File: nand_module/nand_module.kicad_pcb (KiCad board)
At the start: 2 copper layers, 47.1 x 30.9 mm, 19 parts, among them J1 BUS_A, J2 BUS_B

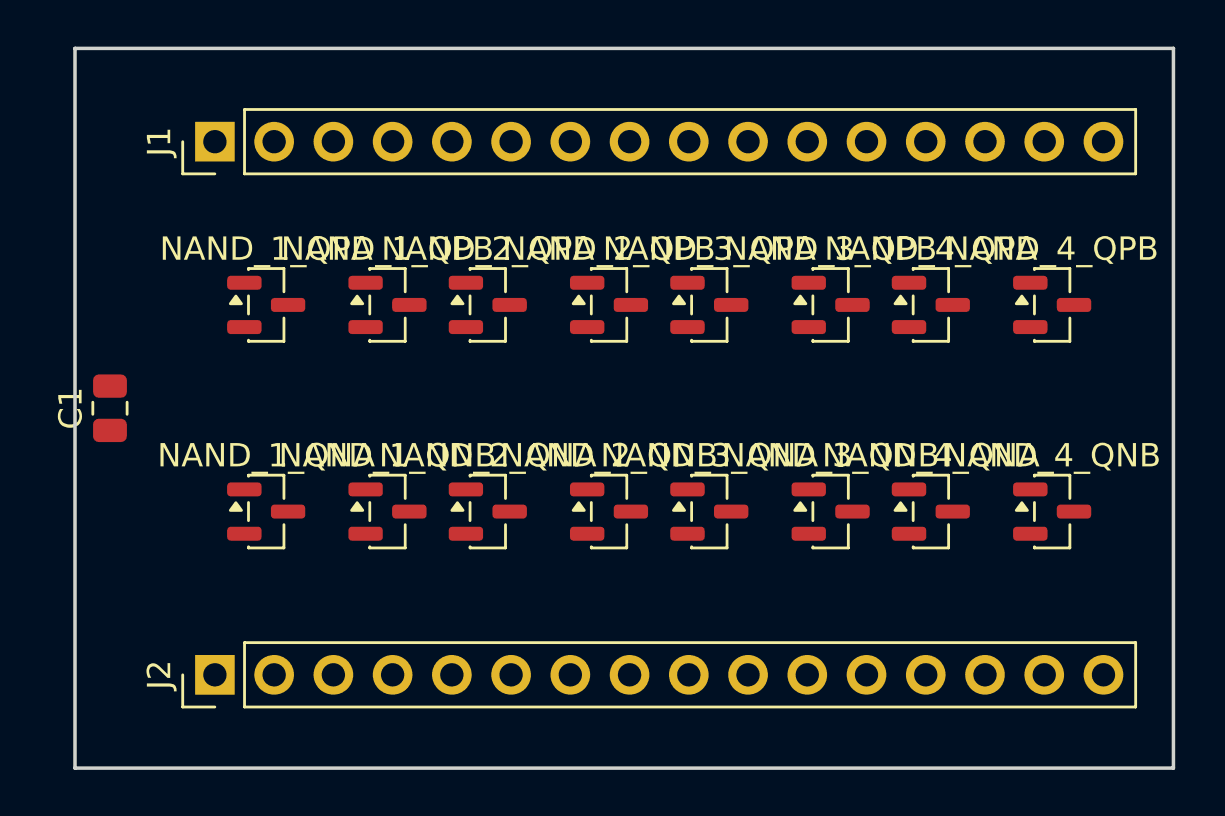
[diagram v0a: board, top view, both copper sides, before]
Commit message: Route NAND module (2-layer, top)
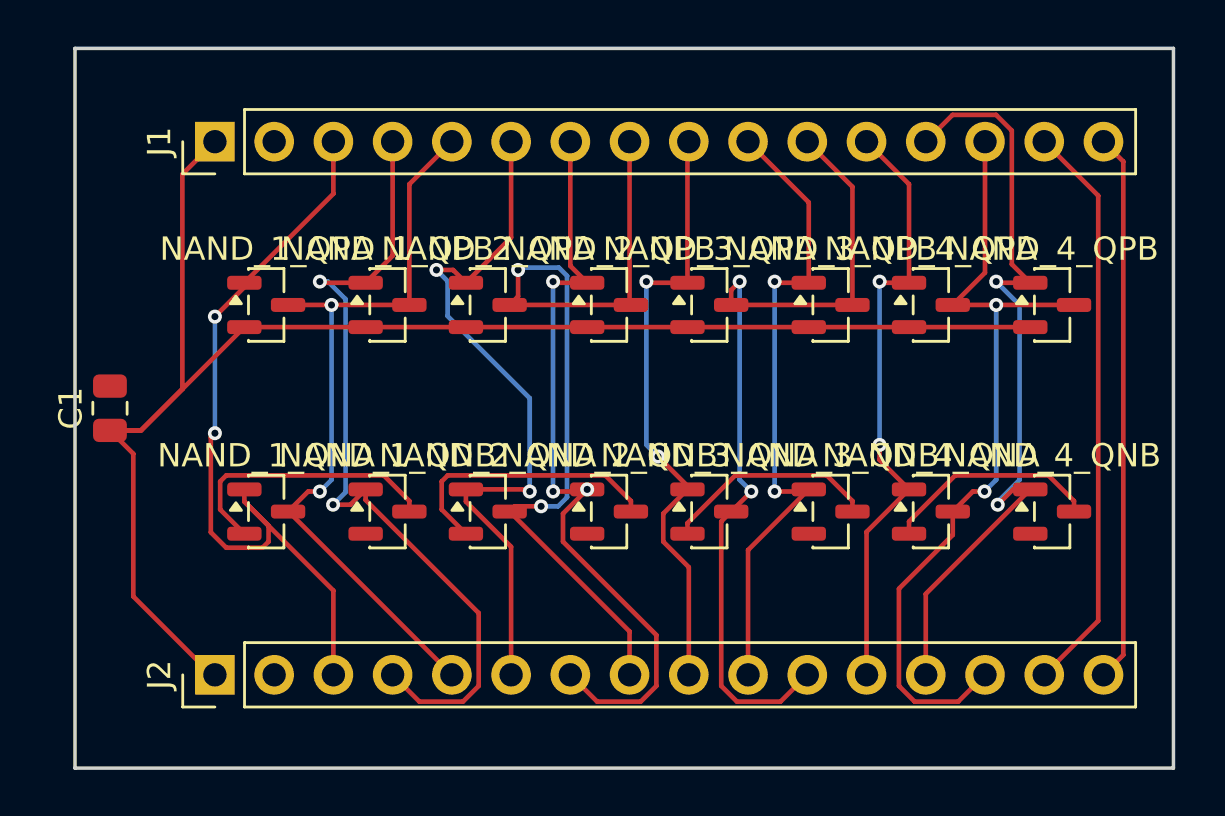
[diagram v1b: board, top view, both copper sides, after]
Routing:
- net VDD: track 0.00 -> 68.7 mm
- net NAND_2_Y: track 0.00 -> 37.5 mm, vias 0 -> 2
- net NAND_3_Y: track 0.00 -> 36.7 mm, vias 0 -> 2
- net NAND_4_Y: track 0.00 -> 35.6 mm, vias 0 -> 2
- net NAND_1_B: track 0.00 -> 35.5 mm, vias 0 -> 2
- net NAND_4_B: track 0.00 -> 34.7 mm, vias 0 -> 2
- net NAND_1_A: track 0.00 -> 33.5 mm, vias 0 -> 2
- net NAND_2_B: track 0.00 -> 33.3 mm, vias 0 -> 3
- net NAND_1_Y: track 0.00 -> 32.8 mm, vias 0 -> 2
- net NAND_2_A: track 0.00 -> 31.0 mm, vias 0 -> 2
- net NAND_3_B: track 0.00 -> 28.1 mm, vias 0 -> 2
- net NAND_3_A: track 0.00 -> 26.3 mm, vias 0 -> 2
- net NAND_4_A: track 0.00 -> 26.2 mm, vias 0 -> 2
- net BUS_X: track 0.00 -> 24.8 mm
- net BUS_Y: track 0.00 -> 23.6 mm
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
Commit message: Rename NAND board refs to short scheme; drop rename_refs.py
Ran rename_refs.py (kept in history at fabc05a) over the routed board:
NAND_<n>_QP*/QN* -> QP*_<n>/QN*_<n>. 240 track objects and all net
names verified unchanged. Also captures routing progress (211 segments).
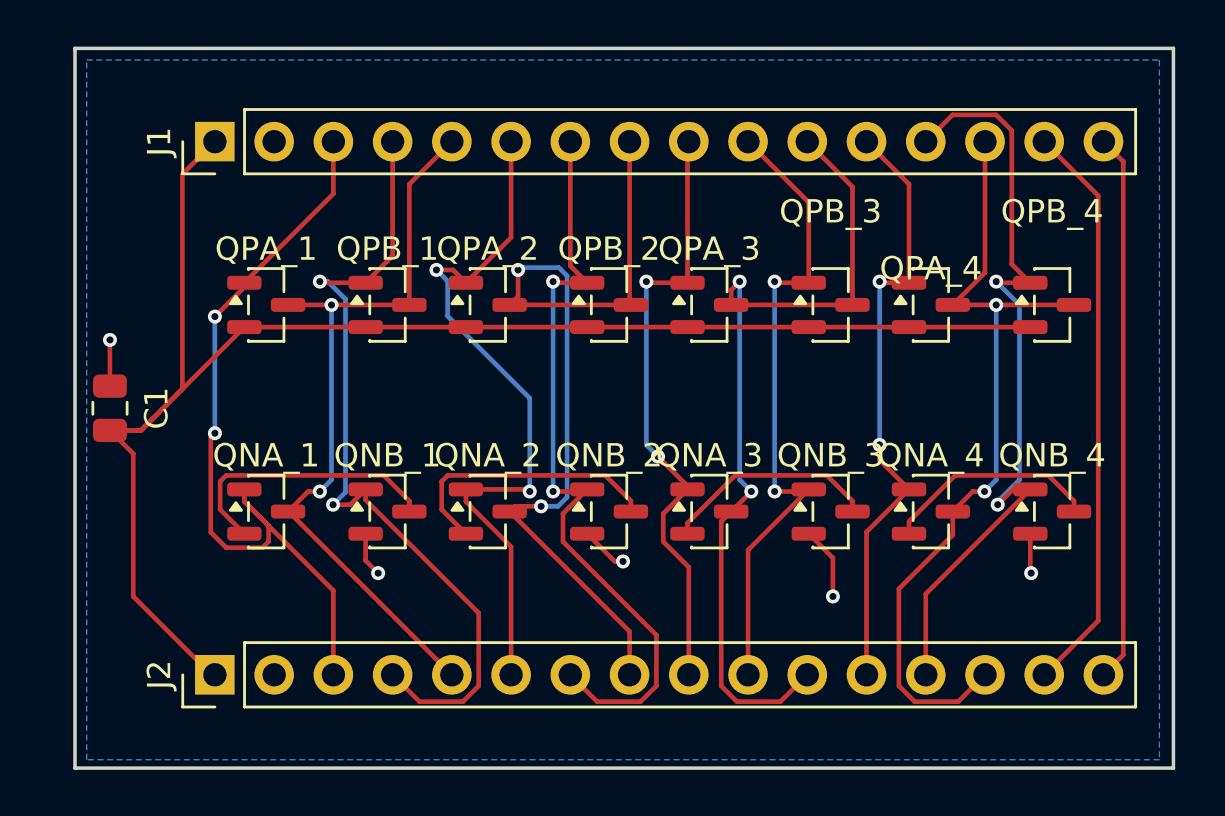
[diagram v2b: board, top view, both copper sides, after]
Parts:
- renumbered NAND_1_QNA to QNA_1, NAND_2_QNA to QNA_2, NAND_3_QNA to QNA_3, NAND_4_QNA to QNA_4, NAND_1_QNB to QNB_1, NAND_2_QNB to QNB_2, NAND_3_QNB to QNB_3, NAND_4_QNB to QNB_4, NAND_1_QPA to QPA_1, NAND_2_QPA to QPA_2, NAND_3_QPA to QPA_3, NAND_4_QPA to QPA_4, NAND_1_QPB to QPB_1, NAND_2_QPB to QPB_2, NAND_3_QPB to QPB_3, NAND_4_QPB to QPB_4
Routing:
- net GND: track 0.00 -> 10.7 mm, vias 0 -> 5
- net NAND_2_B: vias 3 -> 2
- added copper zone on B.Cu, net GND
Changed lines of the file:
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@@
 		(descr "SOT, 3 Pin (JEDEC TO-236 Var AB https://www.jedec.org/document_search?search_api_views_fulltext=TO-236)")
 		(tags "SOT TO_SOT_SMD")
-		(property "Reference" "NAND_2_QPA"
+		(property "Reference" "QPA_2"
 			(at 0 -2.4 0)
 			(layer "F.SilkS")
@@
 		(descr "SOT, 3 Pin (JEDEC TO-236 Var AB https://www.jedec.org/document_search?search_api_views_fulltext=TO-236)")
 		(tags "SOT TO_SOT_SMD")
-		(property "Reference" "NAND_4_QNA"
+		(property "Reference" "QNA_4"
 			(at 0 -2.4 0)
 			(layer "F.SilkS")
@@
 		(descr "SOT, 3 Pin (JEDEC TO-236 Var AB https://www.jedec.org/document_search?search_api_views_fulltext=TO-236)")
 		(tags "SOT TO_SOT_SMD")
-		(property "Reference" "NAND_3_QNB"
+		(property "Reference" "QNB_3"
 			(at 0 -2.4 0)
 			(layer "F.SilkS")
@@
 		(descr "SOT, 3 Pin (JEDEC TO-236 Var AB https://www.jedec.org/document_search?search_api_views_fulltext=TO-236)")
 		(tags "SOT TO_SOT_SMD")
-		(property "Reference" "NAND_2_QNB"
+		(property "Reference" "QNB_2"
 			(at 0 -2.4 0)
 			(layer "F.SilkS")
@@
 		(descr "SOT, 3 Pin (JEDEC TO-236 Var AB https://www.jedec.org/document_search?search_api_views_fulltext=TO-236)")
 		(tags "SOT TO_SOT_SMD")
-		(property "Reference" "NAND_3_QPB"
-			(at 0 -2.4 0)
+		(property "Reference" "QPB_3"
+			(at 0 -4 0)
 			(layer "F.SilkS")
 			(effects
@@
 		(descr "SOT, 3 Pin (JEDEC TO-236 Var AB https://www.jedec.org/document_search?search_api_views_fulltext=TO-236)")
 		(tags "SOT TO_SOT_SMD")
-		(property "Reference" "NAND_1_QNB"
+		(property "Reference" "QNB_1"
 			(at 0 -2.4 0)
 			(layer "F.SilkS")
@@
 		(descr "SOT, 3 Pin (JEDEC TO-236 Var AB https://www.jedec.org/document_search?search_api_views_fulltext=TO-236)")
 		(tags "SOT TO_SOT_SMD")
-		(property "Reference" "NAND_1_QNA"
+		(property "Reference" "QNA_1"
 			(at 0 -2.4 0)
 			(layer "F.SilkS")
@@
 		(descr "SOT, 3 Pin (JEDEC TO-236 Var AB https://www.jedec.org/document_search?search_api_views_fulltext=TO-236)")
 		(tags "SOT TO_SOT_SMD")
-		(property "Reference" "NAND_3_QNA"
+		(property "Reference" "QNA_3"
 			(at 0 -2.4 0)
 			(layer "F.SilkS")
@@
 		(descr "SOT, 3 Pin (JEDEC TO-236 Var AB https://www.jedec.org/document_search?search_api_views_fulltext=TO-236)")
 		(tags "SOT TO_SOT_SMD")
-		(property "Reference" "NAND_1_QPA"
+		(property "Reference" "QPA_1"
 			(at 0 -2.4 0)
 			(layer "F.SilkS")
@@
 		(descr "SOT, 3 Pin (JEDEC TO-236 Var AB https://www.jedec.org/document_search?search_api_views_fulltext=TO-236)")
 		(tags "SOT TO_SOT_SMD")
-		(property "Reference" "NAND_2_QNA"
+		(property "Reference" "QNA_2"
 			(at 0 -2.4 0)
 			(layer "F.SilkS")
@@
 		(descr "SOT, 3 Pin (JEDEC TO-236 Var AB https://www.jedec.org/document_search?search_api_views_fulltext=TO-236)")
 		(tags "SOT TO_SOT_SMD")
-		(property "Reference" "NAND_3_QPA"
+		(property "Reference" "QPA_3"
 			(at 0 -2.4 0)
 			(layer "F.SilkS")
@@
 		(descr "SOT, 3 Pin (JEDEC TO-236 Var AB https://www.jedec.org/document_search?search_api_views_fulltext=TO-236)")
 		(tags "SOT TO_SOT_SMD")
-		(property "Reference" "NAND_4_QNB"
+		(property "Reference" "QNB_4"
 			(at 0 -2.4 0)
 			(layer "F.SilkS")
@@
 		(tags "capacitor")
 		(property "Reference" "C1"
-			(at 0 -1.68 90)
+			(at 0 2 90)
 			(layer "F.SilkS")
 			(effects
@@
 		(descr "SOT, 3 Pin (JEDEC TO-236 Var AB https://www.jedec.org/document_search?search_api_views_fulltext=TO-236)")
 		(tags "SOT TO_SOT_SMD")
-		(property "Reference" "NAND_4_QPA"
-			(at 0 -2.4 0)
+		(property "Reference" "QPA_4"
+			(at 0 -1.56 0)
 			(layer "F.SilkS")
 			(effects
@@
 		(descr "SOT, 3 Pin (JEDEC TO-236 Var AB https://www.jedec.org/document_search?search_api_views_fulltext=TO-236)")
 		(tags "SOT TO_SOT_SMD")
-		(property "Reference" "NAND_1_QPB"
+		(property "Reference" "QPB_1"
 			(at 0 -2.4 0)
 			(layer "F.SilkS")
@@
 		(descr "SOT, 3 Pin (JEDEC TO-236 Var AB https://www.jedec.org/document_search?search_api_views_fulltext=TO-236)")
 		(tags "SOT TO_SOT_SMD")
-		(property "Reference" "NAND_4_QPB"
-			(at 0 -2.4 0)
+		(property "Reference" "QPB_4"
+			(at 0 -4 0)
 			(layer "F.SilkS")
 			(effects
@@
 		(descr "SOT, 3 Pin (JEDEC TO-236 Var AB https://www.jedec.org/document_search?search_api_views_fulltext=TO-236)")
 		(tags "SOT TO_SOT_SMD")
-		(property "Reference" "NAND_2_QPB"
+		(property "Reference" "QPB_2"
 			(at 0 -2.4 0)
 			(layer "F.SilkS")
@@
 	)
 	(segment
+		(start 15.5 30.48)
+		(end 15.5 28.5)
+		(width 0.2)
+		(layer "F.Cu")
+		(net "GND")
+	)
+	(segment
+		(start 37.1525 38)
+		(end 37.5 38)
+		(width 0.2)
+		(layer "F.Cu")
+		(net "GND")
+	)
+	(segment
+		(start 35.9625 36.81)
+		(end 37.1525 38)
+		(width 0.2)
+		(layer "F.Cu")
+		(net "GND")
+	)
+	(segment
+		(start 45.4625 36.81)
+		(end 46.5 37.8475)
+		(width 0.2)
+		(layer "F.Cu")
+		(net "GND")
+	)
+	(segment
+		(start 46.5 37.8475)
+		(end 46.5 39.5)
+		(width 0.2)
+		(layer "F.Cu")
+		(net "GND")
+	)
+	(segment
+		(start 26.4625 37.9625)
+		(end 27 38.5)
+		(width 0.2)
+		(layer "F.Cu")
+		(net "GND")
+	)
+	(segment
+		(start 54.9625 38.4625)
+		(end 55 38.5)
+		(width 0.2)
+		(layer "F.Cu")
+		(net "GND")
+	)
+	(segment
+		(start 26.4625 36.81)
+		(end 26.4625 37.9625)
+		(width 0.2)
+		(layer "F.Cu")
+		(net "GND")
+	)
+	(segment
+		(start 54.9625 36.81)
+		(end 54.9625 38.4625)
+		(width 0.2)
+		(layer "F.Cu")
+		(net "GND")
+	)
+	(via
+		(at 55 38.5)
+		(size 0.6)
+		(drill 0.3)
+		(layers "F.Cu" "B.Cu")
+		(net "GND")
+	)
+	(via
+		(at 15.5 28.5)
+		(size 0.6)
+		(drill 0.3)
+		(layers "F.Cu" "B.Cu")
+		(net "GND")
+	)
+	(via
+		(at 27 38.5)
+		(size 0.6)
+		(drill 0.3)
+		(layers "F.Cu" "B.Cu")
+		(net "GND")
+	)
+	(via
+		(at 37.5 38)
+		(size 0.6)
+		(drill 0.3)
+		(layers "F.Cu" "B.Cu")
+		(net "GND")
+	)
+	(via
+		(at 46.5 39.5)
+		(size 0.6)
+		(drill 0.3)
+		(layers "F.Cu" "B.Cu")
+		(net "GND")
+	)
+	(segment
 		(start 47.3375 35.86)
 		(end 47.3375 35.406948)
@@
 		(net "NAND_2_B")
 	)
-	(via
-		(at 35.9625 34.91)
-		(size 0.6)
-		(drill 0.3)
-		(layers "F.Cu" "B.Cu")
-		(net "NAND_2_B")
-	)
 	(segment
 		(start 34.5 26)
@@
 		(net "BUS_Y")
 	)
+	(zone
+		(net "GND")
+		(layer "B.Cu")
+		(hatch edge 0.5)
+		(connect_pads
+			(clearance 0.5)
+		)
+		(min_thickness 0.25)
+		(fill yes
+			(thermal_gap 0.5)
+			(thermal_bridge_width 0.5)
+			(island_removal_mode 0)
+		)
+		(polygon
+			(pts
+				(xy 14.5 16.5) (xy 60.5 16.5) (xy 60.5 46.5) (xy 14.5 46.5)
+			)
+		)
+	)
 	(embedded_fonts no)

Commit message: Add silkscreen pin labels to NAND board; drop label_headers.py
Ran label_headers.py (kept in history) over the routed board: 28 F.Silks
labels (VDD/GND + 1A..4Y) inside both edge headers. 240 track objects,
refs and net names verified unchanged.
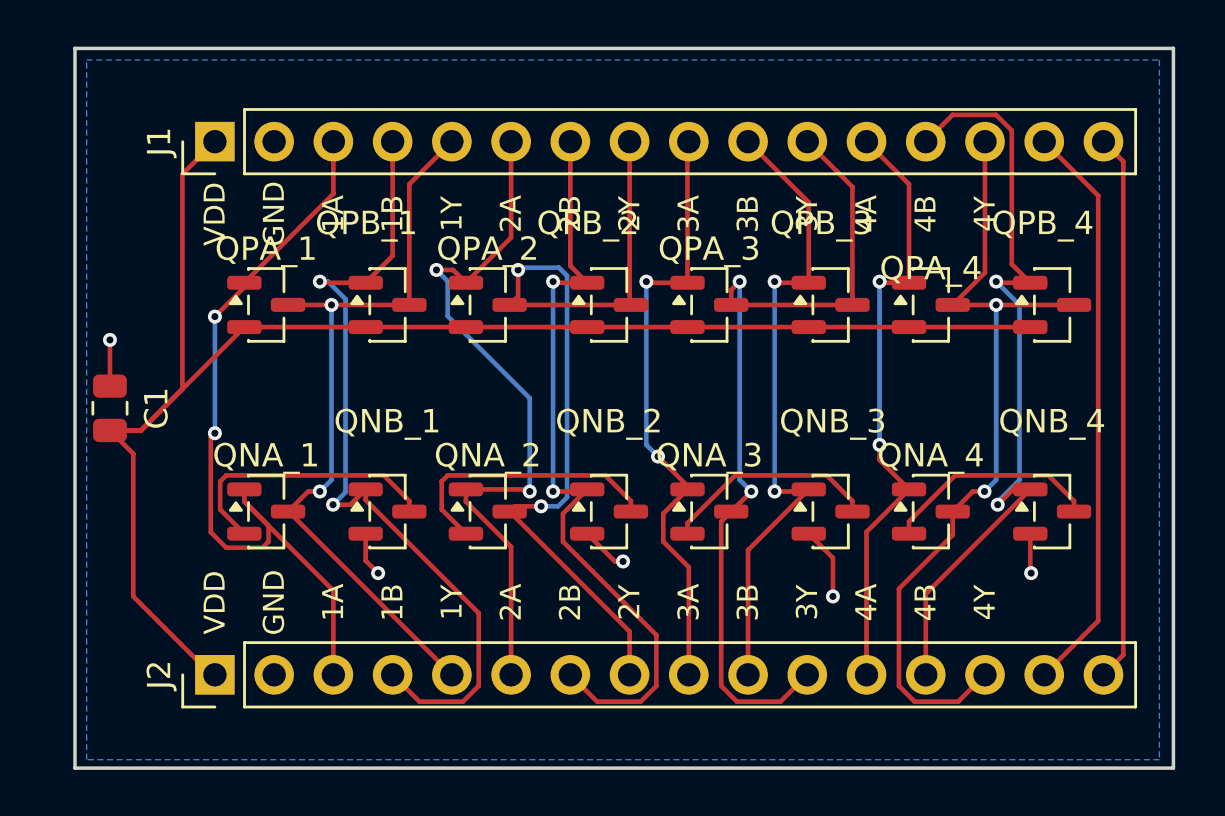
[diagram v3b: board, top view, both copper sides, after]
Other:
- board text added: "1A"
- board text added: "1B"
- board text added: "1Y"
- board text added: "2A"
- board text added: "2B"
- board text added: "2Y"
- board text added: "3A"
- board text added: "3B"
- board text added: "3Y"
- board text added: "4A"
- board text added: "4B"
- board text added: "4Y"
- board text added: "GND"
- board text added: "VDD"
